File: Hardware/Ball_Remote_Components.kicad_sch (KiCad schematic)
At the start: 55 parts, among them J1 I2C_Gyro_Module, J2 USB_B_Micro, J3 SWD_Header, Q1 SI2333DS, SW1 SW_SPDT, U1 MCP73831-2-OT, U2 L3GD20, U3 STM32WB35, U4 LD3985M28R_SOT23, Y1 32MHz, Y2 32.768MHz

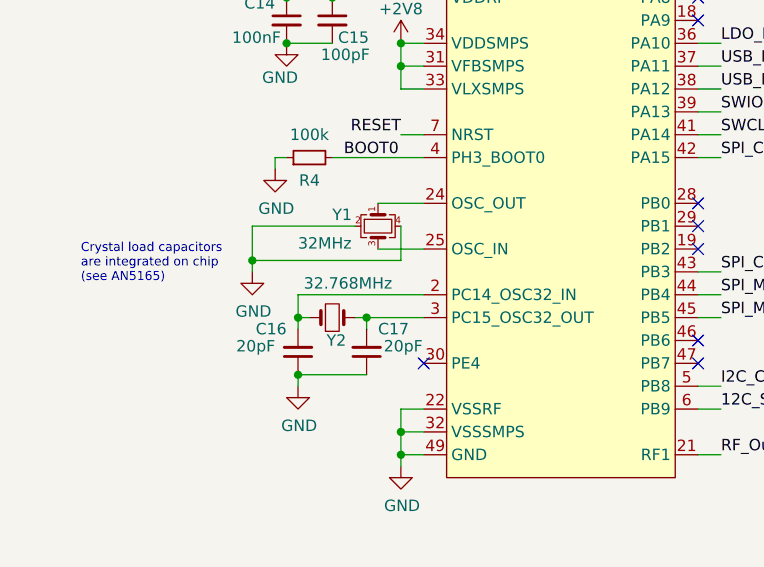
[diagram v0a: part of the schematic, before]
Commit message: Shutdown if battery falls below configurable level
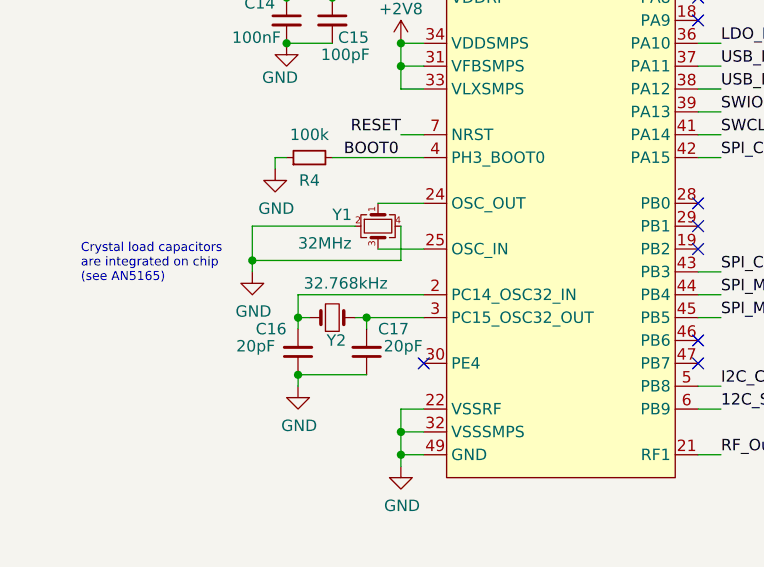
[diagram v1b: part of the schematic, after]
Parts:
- Y2: value 32.768MHz -> 32.768kHz
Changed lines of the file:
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@@
       (effects (font (size 1.27 1.27)) (justify left))
     )
-    (property "Value" "32.768MHz" (at 43.815 86.36 0)
+    (property "Value" "32.768kHz" (at 43.815 86.36 0)
       (effects (font (size 1.27 1.27)) (justify left))
     )

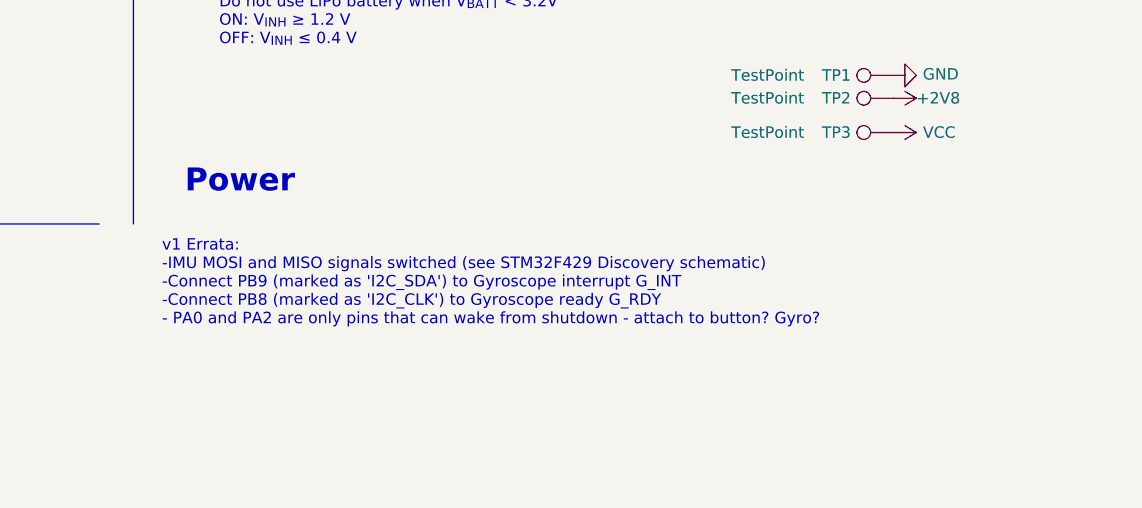
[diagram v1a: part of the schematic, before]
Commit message: Base will periodically wake up remote to check battery level and flash if battery low
Removed offsets from base as handled in remote
Added config for battery warnings and sensitivity
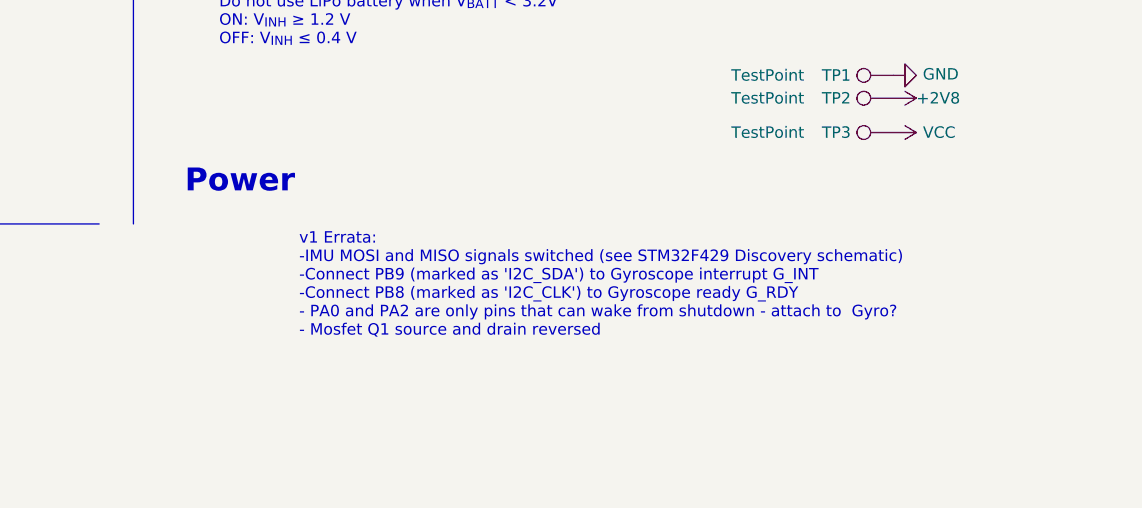
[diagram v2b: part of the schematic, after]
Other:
- note added: "v1 Errata: -IMU MOSI and MISO signals switched (see STM32F429 Discovery schematic) -Connect PB9 (marked as 'I2C_SDA') to Gyroscope interrupt G_INT -Connect PB8 (marked as 'I2C_CLK') to Gyroscope ready G_RDY - PA0 and PA2 are only pins that can wake from shutdown - attach to Gyro? - Mosfet Q1 source and drain reversed"
- note removed: "v1 Errata: -IMU MOSI and MISO signals switched (see STM32F429 Discovery schematic) -Connect PB9 (marked as 'I2C_SDA') to Gyroscope interrupt G_INT -Connect PB8 (marked as 'I2C_CLK') to Gyroscope ready G_RDY - PA0 and PA2 are only pins that can wake from shutdown - attach to button? Gyro?"
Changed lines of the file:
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@@
     (effects (font (size 1.27 1.27)) (justify left bottom))
   )
-  (text "v1 Errata:\n-IMU MOSI and MISO signals switched (see STM32F429 Discovery schematic)\n-Connect PB9 (marked as 'I2C_SDA') to Gyroscope interrupt G_INT\n-Connect PB8 (marked as 'I2C_CLK') to Gyroscope ready G_RDY\n- PA0 and PA2 are only pins that can wake from shutdown - attach to button? Gyro?\n"
-    (at 184.15 177.8 0)
+  (text "v1 Errata:\n-IMU MOSI and MISO signals switched (see STM32F429 Discovery schematic)\n-Connect PB9 (marked as 'I2C_SDA') to Gyroscope interrupt G_INT\n-Connect PB8 (marked as 'I2C_CLK') to Gyroscope ready G_RDY\n- PA0 and PA2 are only pins that can wake from shutdown - attach to  Gyro?\n- Mosfet Q1 source and drain reversed"
+    (at 199.39 179.07 0)
     (effects (font (size 1.27 1.27)) (justify left bottom) (href "#1"))
   )
